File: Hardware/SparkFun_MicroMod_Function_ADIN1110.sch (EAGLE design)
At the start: 93 parts, among them J1 IP20(RJ50), J2 MICROMOD_FUNCTION_STANDARD, Q1 220mA/50V/3.5Ω, Q2 20V/4.2A/52mΩ/1.4W, T1 WE-STST, U1 ADIN1110, U2 EEPROM, U3 3.3V, U4 WE-TVS, Y1 25MHz

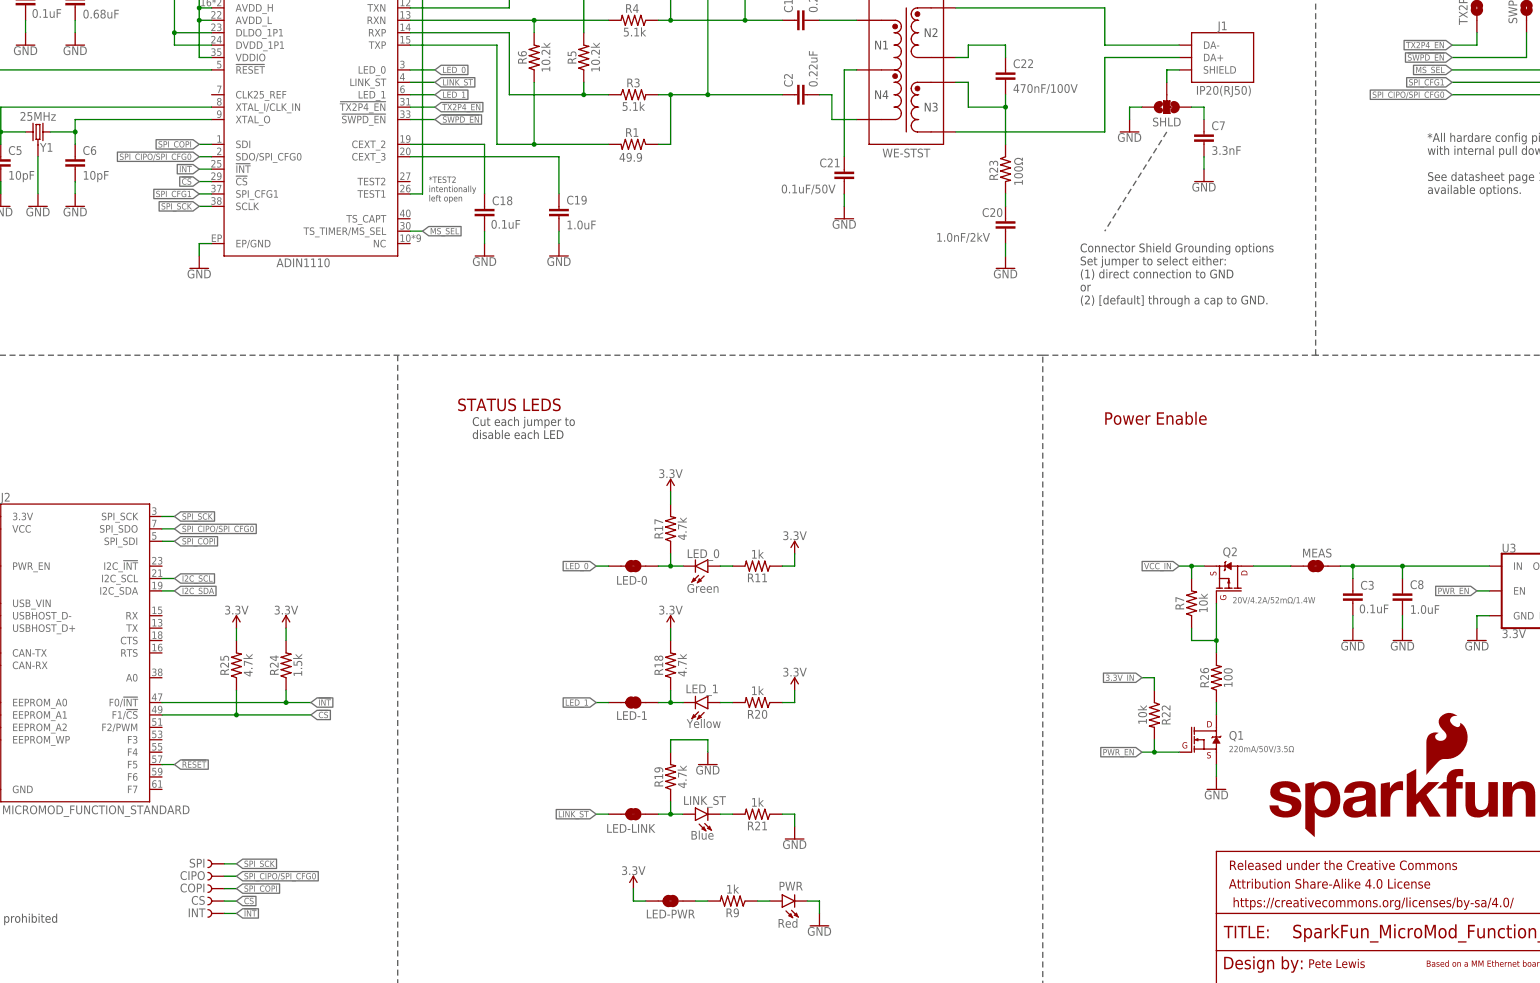
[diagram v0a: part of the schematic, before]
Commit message: Renaming CIPO/COPI to POCI/PICO
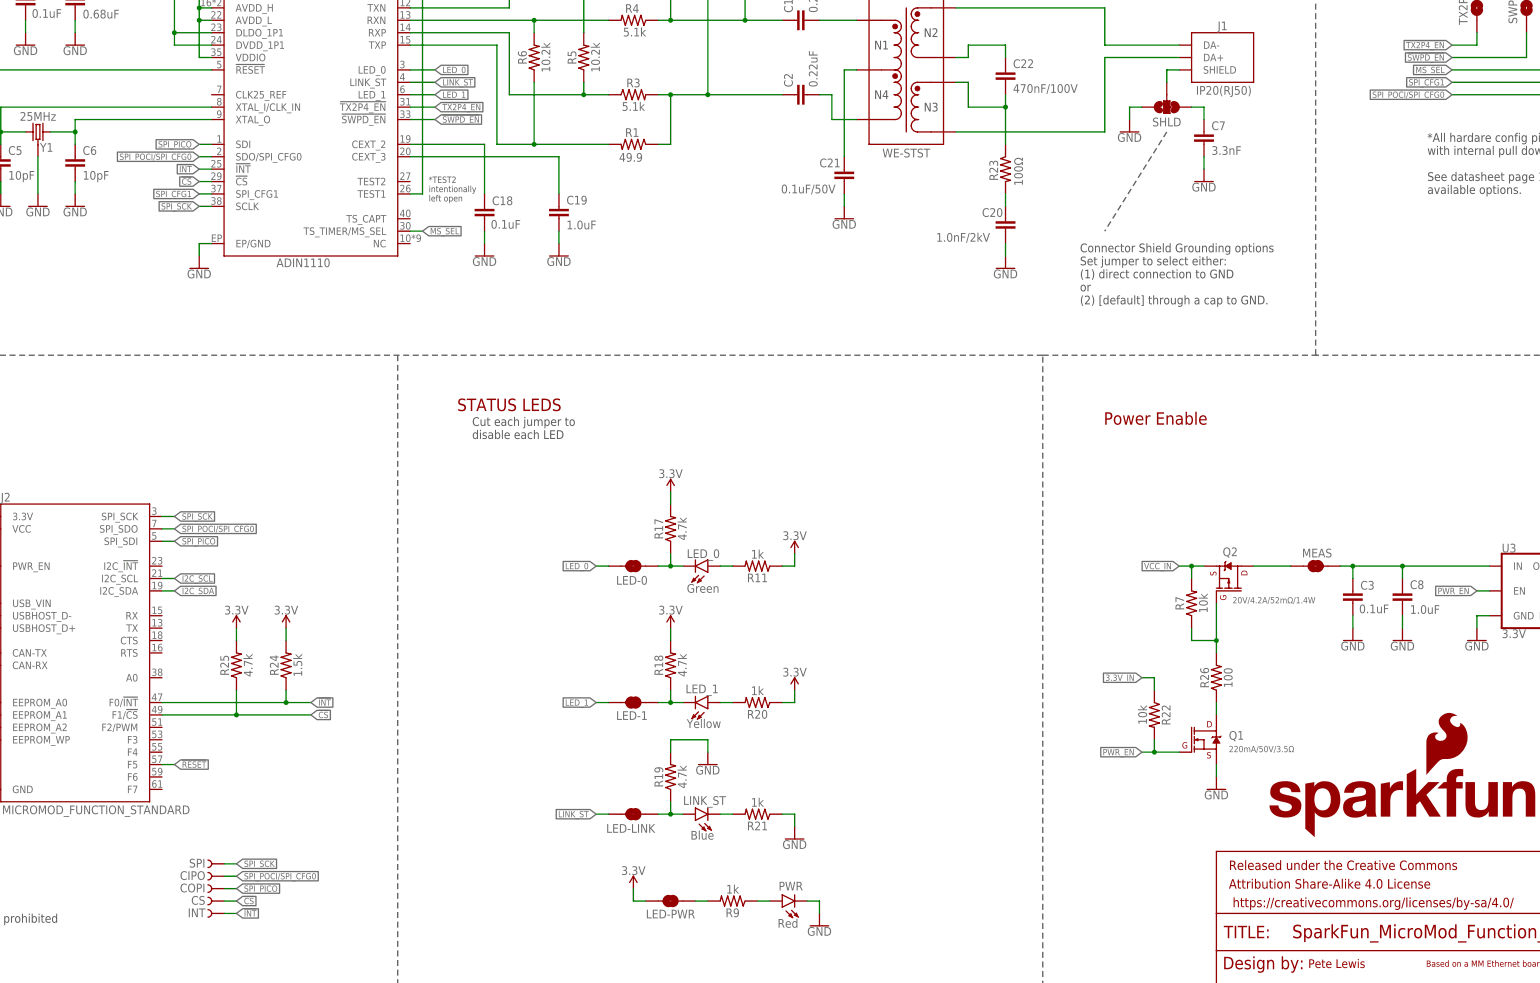
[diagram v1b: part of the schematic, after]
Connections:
- net SPI_CIPO/SPI_CFG0 renamed SPI_POCI/SPI_CFG0
- net SPI_COPI renamed SPI_PICO
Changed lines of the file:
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@@
 </segment>
 </net>
-<net name="SPI_COPI" class="0">
+<net name="SPI_PICO" class="0">
 <segment>
 <wire x1="114.3" y1="99.06" x2="116.84" y2="99.06" width="0.1524" layer="91"/>
@@
 </segment>
 </net>
-<net name="SPI_CIPO/SPI_CFG0" class="0">
+<net name="SPI_POCI/SPI_CFG0" class="0">
 <segment>
 <wire x1="114.3" y1="101.6" x2="116.84" y2="101.6" width="0.1524" layer="91"/>

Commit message: PROD_ID for 0.68uF 0603 Cap (C11)
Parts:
- C11: device SparkFun-Capacitors:CAP-0603 -> SparkFun-Capacitors:0.68UF-0603-16V-10%-X7R-WE
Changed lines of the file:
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@@
 <part name="C10" library="SparkFun-Capacitors" deviceset="0.1UF" device="-0402T-16V-10%-X7R-WE" value="0.1uF"/>
 <part name="GND36" library="SparkFun-PowerSymbols" deviceset="GND" device=""/>
-<part name="C11" library="SparkFun-Capacitors" deviceset="CAP" device="-0603" value="0.68uF"/>
+<part name="C11" library="SparkFun-Capacitors" deviceset="0.68UF" device="-0603-16V-10%-X7R-WE" value="0.68uF"/>
 <part name="GND37" library="SparkFun-PowerSymbols" deviceset="GND" device=""/>
 <part name="C12" library="SparkFun-Capacitors" deviceset="10NF" device="-0402T-25V-10%-X7R-WE" value="10nF"/>

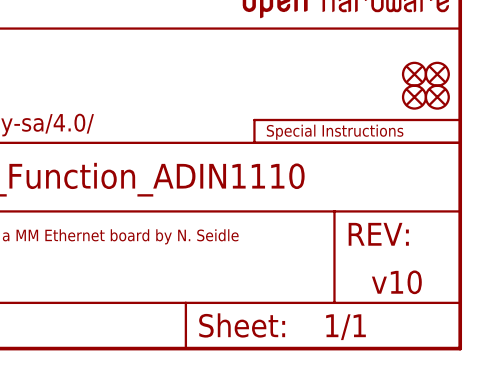
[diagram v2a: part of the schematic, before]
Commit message: Silk updated to "Single Pair Ethernet"
-updated product name silk
-bumped version to v11 in brd and sch
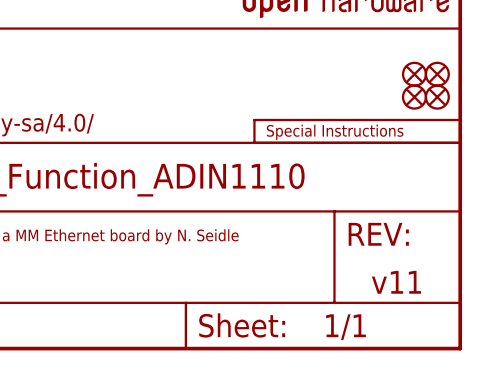
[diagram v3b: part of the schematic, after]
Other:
- note added: "v11"
- note removed: "v10"
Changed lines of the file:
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@@
 <text x="30.734" y="126.746" size="2.54" layer="94" font="vector" ratio="12" align="center">MicroMod Function Connector</text>
 <text x="348.996" y="11.684" size="1.778" layer="94" font="vector">Pete Lewis</text>
-<text x="421.894" y="6.096" size="2.54" layer="94" font="vector">v10</text>
+<text x="421.894" y="6.096" size="2.54" layer="94" font="vector">v11</text>
 <text x="45.72" y="271.78" size="2.54" layer="94" font="vector" ratio="12" align="center">ADIN1110 BASE10-T1L ETHERNET MAC-PHY</text>
 <text x="317.754" y="124.206" size="2.54" layer="94" font="vector" ratio="12" align="center">Power Enable</text>

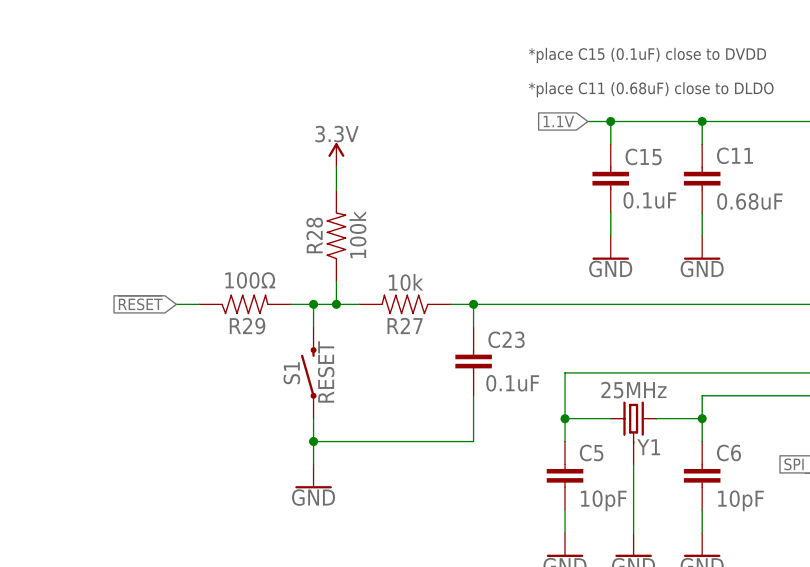
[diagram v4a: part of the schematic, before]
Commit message: R27 changed to 4.7K
-updated prod_id and values on boat single and panel files.
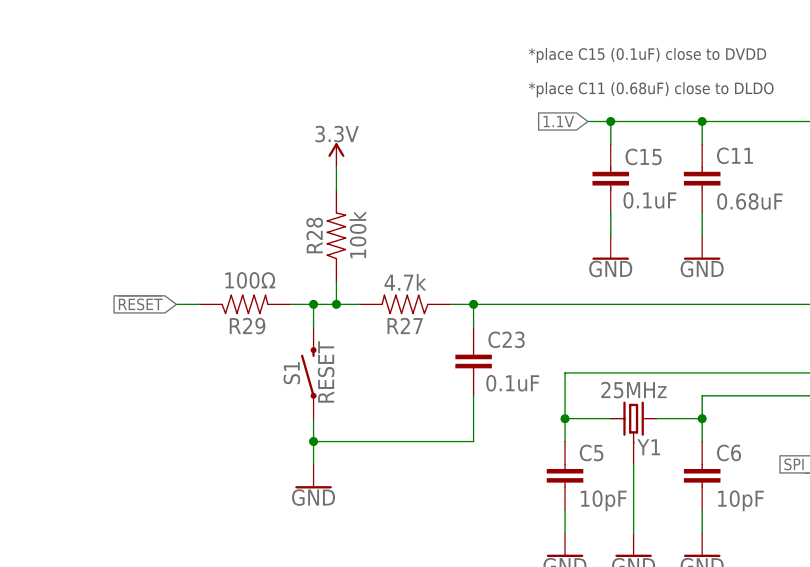
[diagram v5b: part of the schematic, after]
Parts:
- R27: value 10k -> 4.7k; device SparkFun-Resistors:10KOHM-0603-1/10W-1% -> SparkFun-Resistors:4.7KOHM-0603-1/10W-1%
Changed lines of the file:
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@@
 <part name="GND15" library="SparkFun-PowerSymbols" deviceset="GND" device=""/>
 <part name="R26" library="SparkFun-Resistors" deviceset="100OHM" device="-0603-1/10W-1%" value="100"/>
-<part name="R27" library="SparkFun-Resistors" deviceset="10KOHM" device="-0603-1/10W-1%" value="10k"/>
+<part name="R27" library="SparkFun-Resistors" deviceset="4.7KOHM" device="-0603-1/10W-1%" value="4.7k"/>
 <part name="SUPPLY4" library="SparkFun-PowerSymbols" deviceset="3.3V" device=""/>
 <part name="R28" library="SparkFun-Resistors" deviceset="100KOHM" device="-0402T-1/16W-1%" value="100k"/>

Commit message: v12 - partner logos added
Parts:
- added U$19: WURTH_LOGO, temp_logos:WURTH_LOGO
- added U$2: HARTING_LOGO, temp_logos:HARTING_LOGO
- added U$33: ANALOG_DEVICES_LOGO, temp_logos:ANALOG_DEVICES_LOGO
- added U$5: DIGIKEY_LOGO, temp_logos:DIGIKEY_LOGO
- LOGO1: value SFE_LOGO_NAME_FLAME.2_INCH -> SFE_LOGO_NAME_FLAME.1_INCH; device SparkFun-Aesthetics:SFE_LOGO_NAME_FLAME.2_INCH -> SparkFun-Aesthetics:SFE_LOGO_NAME_FLAME.1_INCH
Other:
- note added: "v12"
- note removed: "v11"
- moved on the sheet: C3, C4, C8, C9, EWP, LED-0, LED-1, LED-LINK, LED-PWR, LED_0, LED_1, LINK_ST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
